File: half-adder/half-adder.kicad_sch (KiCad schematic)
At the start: 15 parts, among them J1 A, J2 B, J3 C, J4 5V, J5 GROUND, J6 CARRY OUT, J7 OUTPUT

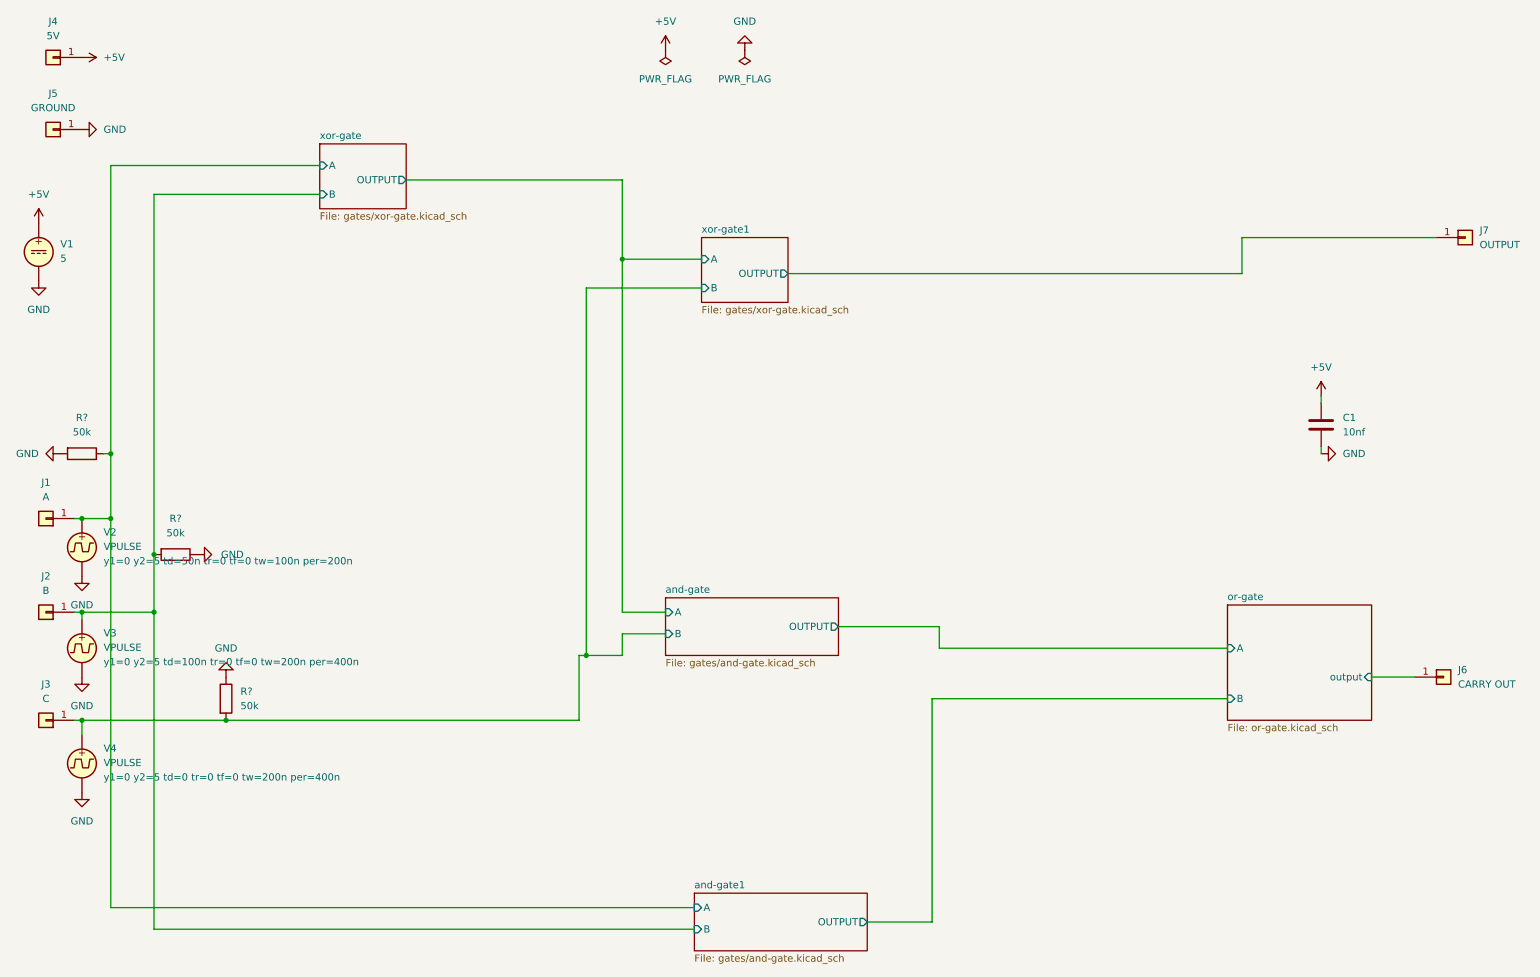
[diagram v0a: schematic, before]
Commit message: Fixed gates and moved half adder to its own directory
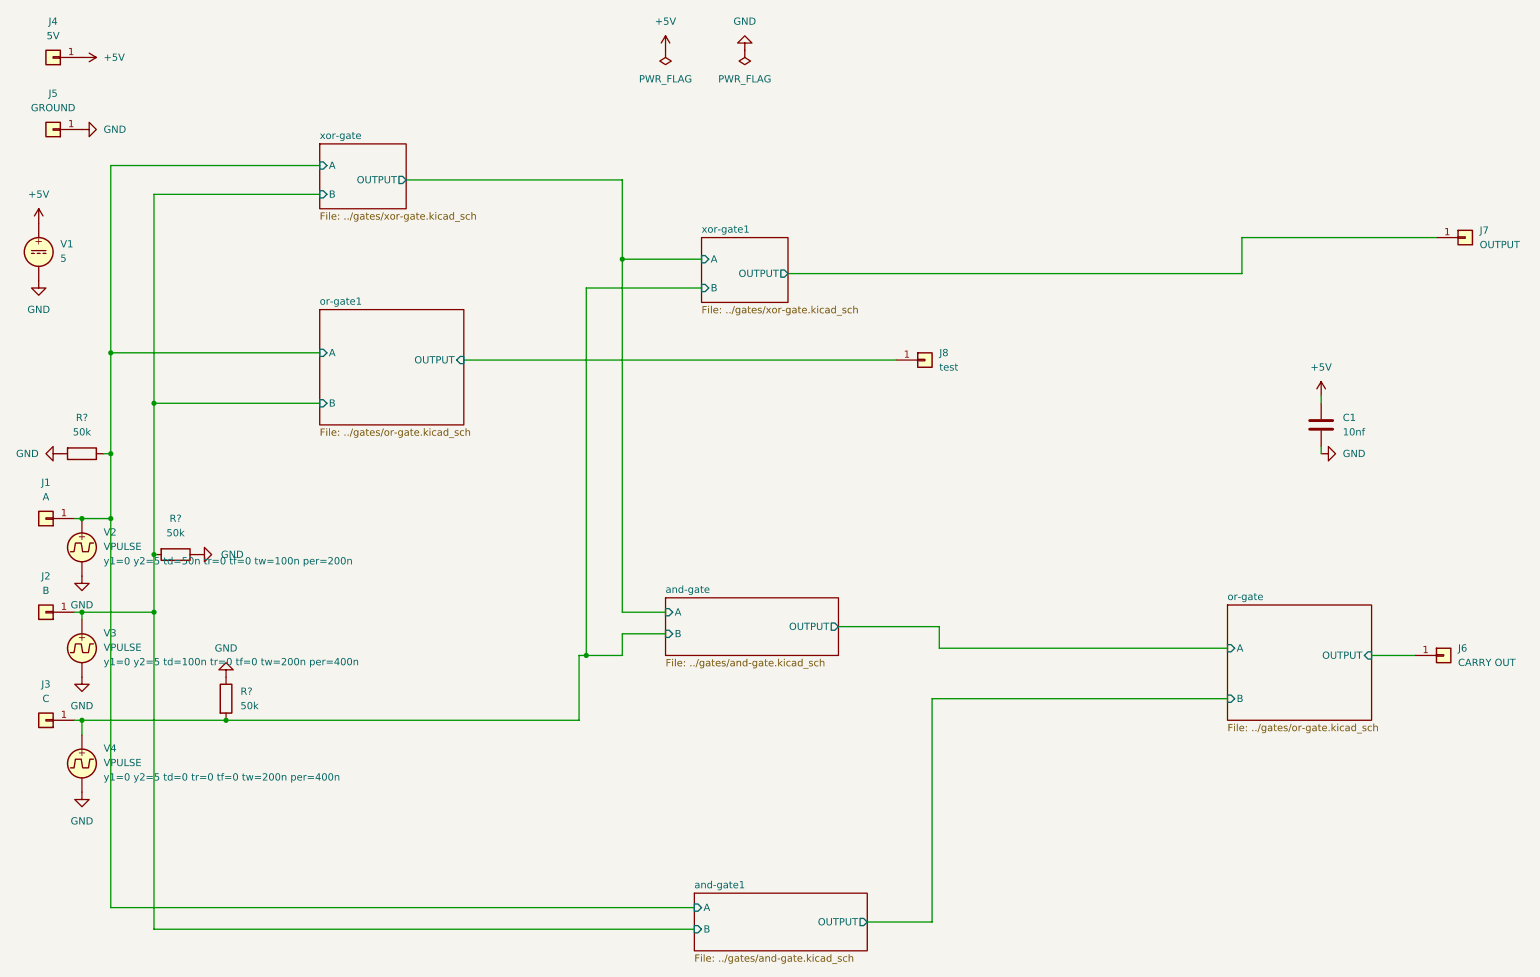
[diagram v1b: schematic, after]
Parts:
- added J8: test, Connector_PinHeader_2.54mm:PinHeader_1x01_P2.54mm_Vertical, symbol Connector_Generic:Conn_01x01
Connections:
- net or-gate/output renamed or-gate/OUTPUT
- new net or-gate1/OUTPUT: J8.1 (Pin_1)
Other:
- added sheet or-gate1 (../gates/or-gate.kicad_sch)
- sheet and-gate: file gates/and-gate.kicad_sch -> ../gates/and-gate.kicad_sch
- sheet and-gate1: file gates/and-gate.kicad_sch -> ../gates/and-gate.kicad_sch
- sheet or-gate: file or-gate.kicad_sch -> ../gates/or-gate.kicad_sch
- sheet or-gate ports: added OUTPUT; removed output
- sheet xor-gate: file gates/xor-gate.kicad_sch -> ../gates/xor-gate.kicad_sch
- sheet xor-gate1: file gates/xor-gate.kicad_sch -> ../gates/xor-gate.kicad_sch
- moved on the sheet: J6
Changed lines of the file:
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@@
 	)
 	(junction
+		(at 30.48 74.93)
+		(diameter 0)
+		(color 0 0 0 0)
+	)
+	(junction
 		(at 25.4 120.65)
 		(diameter 0)
@@
 	)
 	(junction
+		(at 38.1 83.82)
+		(diameter 0)
+		(color 0 0 0 0)
+	)
+	(junction
 		(at 114.3 128.27)
 		(diameter 0)
@@
 	(wire
 		(pts
-			(xy 38.1 46.99) (xy 38.1 110.49)
+			(xy 30.48 172.72) (xy 133.35 172.72)
 		)
 		(stroke
@@
 	(wire
 		(pts
-			(xy 30.48 172.72) (xy 133.35 172.72)
+			(xy 229.87 60.96) (xy 229.87 54.61)
 		)
 		(stroke
@@
 	(wire
 		(pts
-			(xy 229.87 60.96) (xy 229.87 54.61)
+			(xy 30.48 41.91) (xy 67.31 41.91)
 		)
 		(stroke
@@
 	(wire
 		(pts
-			(xy 30.48 41.91) (xy 67.31 41.91)
+			(xy 38.1 120.65) (xy 38.1 176.53)
 		)
 		(stroke
@@
 	(wire
 		(pts
-			(xy 38.1 120.65) (xy 38.1 176.53)
+			(xy 175.26 135.89) (xy 227.33 135.89)
 		)
 		(stroke
@@
 	(wire
 		(pts
-			(xy 175.26 135.89) (xy 227.33 135.89)
+			(xy 30.48 41.91) (xy 30.48 74.93)
 		)
 		(stroke
@@
 	(wire
 		(pts
-			(xy 30.48 41.91) (xy 30.48 92.71)
+			(xy 38.1 83.82) (xy 38.1 110.49)
 		)
 		(stroke
@@
 	(wire
 		(pts
+			(xy 67.31 74.93) (xy 30.48 74.93)
+		)
+		(stroke
+			(width 0)
+			(type default)
+		)
+	)
+	(wire
+		(pts
 			(xy 114.3 128.27) (xy 120.65 128.27)
 		)
@@
 	(wire
 		(pts
+			(xy 92.71 76.2) (xy 168.91 76.2)
+		)
+		(stroke
+			(width 0)
+			(type default)
+		)
+	)
+	(wire
+		(pts
 			(xy 50.8 139.7) (xy 113.03 139.7)
 		)
@@
 	(wire
 		(pts
-			(xy 252.73 132.08) (xy 260.35 132.08)
+			(xy 252.73 128.27) (xy 260.35 128.27)
 		)
 		(stroke
@@
 	(wire
 		(pts
+			(xy 38.1 83.82) (xy 67.31 83.82)
+		)
+		(stroke
+			(width 0)
+			(type default)
+		)
+	)
+	(wire
+		(pts
 			(xy 120.65 58.42) (xy 134.62 58.42)
 		)
@@
 	(wire
 		(pts
+			(xy 38.1 46.99) (xy 38.1 83.82)
+		)
+		(stroke
+			(width 0)
+			(type default)
+		)
+	)
+	(wire
+		(pts
 			(xy 25.4 120.65) (xy 38.1 120.65)
 		)
@@
 	(wire
 		(pts
+			(xy 30.48 74.93) (xy 30.48 92.71)
+		)
+		(stroke
+			(width 0)
+			(type default)
+		)
+	)
+	(wire
+		(pts
 			(xy 243.84 82.55) (xy 243.84 83.82)
 		)
@@
 	)
 	(symbol
+		(lib_id "Connector_Generic:Conn_01x01")
+		(at 173.99 76.2 0)
+		(unit 1)
+		(exclude_from_sim yes)
+		(in_bom yes)
+		(on_board yes)
+		(dnp no)
+		(fields_autoplaced yes)
+		(property "Reference" "J8"
+			(at 176.53 74.93 0)
+			(effects
+				(font
+					(size 1.27 1.27)
+				)
+				(justify left)
+			)
+		)
+		(property "Value" "test"
+			(at 176.53 77.47 0)
+			(effects
+				(font
+					(size 1.27 1.27)
+				)
+				(justify left)
+			)
+		)
+		(property "Footprint" "Connector_PinHeader_2.54mm:PinHeader_1x01_P2.54mm_Vertical"
+			(at 173.99 76.2 0)
+			(effects
+				(font
+					(size 1.27 1.27)
+				)
+				(hide yes)
+			)
+		)
+		(property "Datasheet" "~"
+			(at 173.99 76.2 0)
+			(effects
+				(font
+					(size 1.27 1.27)
+				)
+				(hide yes)
+			)
+		)
+		(property "Description" ""
+			(at 173.99 76.2 0)
+			(effects
+				(font
+					(size 1.27 1.27)
+				)
+				(hide yes)
+			)
+		)
+		(property "LCSC" ""
+			(at 173.99 76.2 0)
+			(effects
+				(font
+					(size 1.27 1.27)
+				)
+				(hide yes)
+			)
+		)
+		(pin "1"
+		)
+		(instances
+			(project "half-adder"
+				(path "/88c27409-0a88-4cf1-8b65-cf7271709e32"
+					(reference "J8")
+					(unit 1)
+				)
+			)
+		)
+	)
+	(symbol
 		(lib_id "power:+5V")
 		(at 25.4 22.86 270)
@@
 	(symbol
 		(lib_id "Connector_Generic:Conn_01x01")
-		(at 265.43 132.08 0)
+		(at 265.43 128.27 0)
 		(unit 1)
 		(exclude_from_sim yes)
@@
 		(fields_autoplaced yes)
 		(property "Reference" "J6"
-			(at 267.97 130.81 0)
+			(at 267.97 127 0)
 			(effects
 				(font
@@
 		)
 		(property "Value" "CARRY OUT"
-			(at 267.97 133.35 0)
+			(at 267.97 129.54 0)
 			(effects
 				(font
@@
 		)
 		(property "Footprint" "Connector_PinHeader_2.54mm:PinHeader_1x01_P2.54mm_Vertical"
-			(at 265.43 132.08 0)
+			(at 265.43 128.27 0)
 			(effects
 				(font
@@
 		)
 		(property "Datasheet" "~"
-			(at 265.43 132.08 0)
+			(at 265.43 128.27 0)
 			(effects
 				(font
@@
 		)
 		(property "Description" ""
-			(at 265.43 132.08 0)
+			(at 265.43 128.27 0)
 			(effects
 				(font
@@
 		)
 		(property "LCSC" ""
-			(at 265.43 132.08 0)
+			(at 265.43 128.27 0)
 			(effects
 				(font
@@
 			)
 		)
-		(property "Sheetfile" "gates/and-gate.kicad_sch"
+		(property "Sheetfile" "../gates/and-gate.kicad_sch"
 			(at 133.35 180.9246 0)
 			(effects
@@
 	)
 	(sheet
-		(at 227.33 119.38)
+		(at 67.31 67.31)
 		(size 25.4 20.32)
 		(fields_autoplaced yes)
@@
 			(color 0 0 0 0.0000)
 		)
-		(property "Sheetname" "or-gate"
-			(at 227.33 118.6684 0)
+		(property "Sheetname" "or-gate1"
+			(at 67.31 66.5984 0)
 			(effects
 				(font
@@
 			)
 		)
-		(property "Sheetfile" "or-gate.kicad_sch"
-			(at 227.33 140.2846 0)
+		(property "Sheetfile" "../gates/or-gate.kicad_sch"
+			(at 67.31 88.2146 0)
 			(effects
 				(font
@@
 			)
 		)
-		(pin "output" input
-			(at 252.73 132.08 0)
+		(pin "A" input
+			(at 67.31 74.93 180)
+			(effects
+				(font
+					(size 1.27 1.27)
+				)
+				(justify left)
+			)
+		)
+		(pin "B" input
+			(at 67.31 83.82 180)
+			(effects
+				(font
+					(size 1.27 1.27)
+				)
+				(justify left)
+			)
+		)
+		(pin "OUTPUT" input
+			(at 92.71 76.2 0)
 			(effects
 				(font
@@
 			)
 		)
+		(instances
+			(project "half-adder"
+				(path "/88c27409-0a88-4cf1-8b65-cf7271709e32"
+					(page "13")
+				)
+			)
+		)
+	)
+	(sheet
+		(at 227.33 119.38)
+		(size 25.4 20.32)
+		(fields_autoplaced yes)
+		(stroke
+			(width 0.1524)
+			(type solid)
+		)
+		(fill
+			(color 0 0 0 0.0000)
+		)
+		(property "Sheetname" "or-gate"
+			(at 227.33 118.6684 0)
+			(effects
+				(font
+					(size 1.27 1.27)
+				)
+				(justify left bottom)
+			)
+		)
+		(property "Sheetfile" "../gates/or-gate.kicad_sch"
+			(at 227.33 140.2846 0)
+			(effects
+				(font
+					(size 1.27 1.27)
+				)
+				(justify left top)
+			)
+		)
 		(pin "A" input
 			(at 227.33 127 180)
@@
 			)
 		)
+		(pin "OUTPUT" input
+			(at 252.73 128.27 0)
+			(effects
+				(font
+					(size 1.27 1.27)
+				)
+				(justify right)
+			)
+		)
 		(instances
 			(project "half-adder"
@@
 			)
 		)
-		(property "Sheetfile" "gates/xor-gate.kicad_sch"
+		(property "Sheetfile" "../gates/xor-gate.kicad_sch"
 			(at 67.31 50.1146 0)
 			(effects
@@
 			)
 		)
-		(property "Sheetfile" "gates/xor-gate.kicad_sch"
+		(property "Sheetfile" "../gates/xor-gate.kicad_sch"
 			(at 134.62 66.6246 0)
 			(effects
@@
 			)
 		)
-		(property "Sheetfile" "gates/and-gate.kicad_sch"
+		(property "Sheetfile" "../gates/and-gate.kicad_sch"
 			(at 128.27 128.8546 0)
 			(effects

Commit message: Remove unneeded or gate
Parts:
- removed J8: test, Connector_PinHeader_2.54mm:PinHeader_1x01_P2.54mm_Vertical, symbol Connector_Generic:Conn_01x01
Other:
- removed sheet or-gate1
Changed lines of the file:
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@@
-	)
-	(junction
-		(at 30.48 74.93)
-		(diameter 0)
-		(color 0 0 0 0)
 	)
 	(junction
@@
 	)
 	(junction
-		(at 38.1 83.82)
-		(diameter 0)
-		(color 0 0 0 0)
-	)
-	(junction
 		(at 114.3 128.27)
 		(diameter 0)
@@
 	(wire
 		(pts
-			(xy 30.48 41.91) (xy 30.48 74.93)
+			(xy 30.48 41.91) (xy 30.48 92.71)
 		)
 		(stroke
@@
 	(wire
 		(pts
-			(xy 38.1 83.82) (xy 38.1 110.49)
+			(xy 38.1 46.99) (xy 38.1 110.49)
 		)
 		(stroke
@@
 	(wire
 		(pts
-			(xy 67.31 74.93) (xy 30.48 74.93)
-		)
-		(stroke
-			(width 0)
-			(type default)
-		)
-	)
-	(wire
-		(pts
 			(xy 114.3 128.27) (xy 120.65 128.27)
 		)
@@
 	(wire
 		(pts
-			(xy 92.71 76.2) (xy 168.91 76.2)
-		)
-		(stroke
-			(width 0)
-			(type default)
-		)
-	)
-	(wire
-		(pts
 			(xy 50.8 139.7) (xy 113.03 139.7)
 		)
@@
 	(wire
 		(pts
-			(xy 38.1 83.82) (xy 67.31 83.82)
-		)
-		(stroke
-			(width 0)
-			(type default)
-		)
-	)
-	(wire
-		(pts
 			(xy 120.65 58.42) (xy 134.62 58.42)
 		)
@@
 	(wire
 		(pts
-			(xy 38.1 46.99) (xy 38.1 83.82)
-		)
-		(stroke
-			(width 0)
-			(type default)
-		)
-	)
-	(wire
-		(pts
 			(xy 25.4 120.65) (xy 38.1 120.65)
 		)
@@
 		(pts
 			(xy 38.1 176.53) (xy 133.35 176.53)
-		)
-		(stroke
-			(width 0)
-			(type default)
-		)
-	)
-	(wire
-		(pts
-			(xy 30.48 74.93) (xy 30.48 92.71)
 		)
 		(stroke
@@
 	)
 	(symbol
-		(lib_id "Connector_Generic:Conn_01x01")
-		(at 173.99 76.2 0)
-		(unit 1)
-		(exclude_from_sim yes)
-		(in_bom yes)
-		(on_board yes)
-		(dnp no)
-		(fields_autoplaced yes)
-		(property "Reference" "J8"
-			(at 176.53 74.93 0)
-			(effects
-				(font
-					(size 1.27 1.27)
-				)
-				(justify left)
-			)
-		)
-		(property "Value" "test"
-			(at 176.53 77.47 0)
-			(effects
-				(font
-					(size 1.27 1.27)
-				)
-				(justify left)
-			)
-		)
-		(property "Footprint" "Connector_PinHeader_2.54mm:PinHeader_1x01_P2.54mm_Vertical"
-			(at 173.99 76.2 0)
-			(effects
-				(font
-					(size 1.27 1.27)
-				)
-				(hide yes)
-			)
-		)
-		(property "Datasheet" "~"
-			(at 173.99 76.2 0)
-			(effects
-				(font
-					(size 1.27 1.27)
-				)
-				(hide yes)
-			)
-		)
-		(property "Description" ""
-			(at 173.99 76.2 0)
-			(effects
-				(font
-					(size 1.27 1.27)
-				)
-				(hide yes)
-			)
-		)
-		(property "LCSC" ""
-			(at 173.99 76.2 0)
-			(effects
-				(font
-					(size 1.27 1.27)
-				)
-				(hide yes)
-			)
-		)
-		(pin "1"
-		)
-		(instances
-			(project "half-adder"
-				(path "/88c27409-0a88-4cf1-8b65-cf7271709e32"
-					(reference "J8")
-					(unit 1)
-				)
-			)
-		)
-	)
-	(symbol
 		(lib_id "power:+5V")
 		(at 25.4 22.86 270)
@@
 				)
 			)
-		)
-	)
-	(sheet
-		(at 67.31 67.31)
-		(size 25.4 20.32)
-		(fields_autoplaced yes)
-		(stroke
-			(width 0.1524)
-			(type solid)
-		)
-		(fill
-			(color 0 0 0 0.0000)
-		)
-		(property "Sheetname" "or-gate1"
-			(at 67.31 66.5984 0)
-			(effects
-				(font
-					(size 1.27 1.27)
-				)
-				(justify left bottom)
-			)
-		)
-		(property "Sheetfile" "../gates/or-gate.kicad_sch"
-			(at 67.31 88.2146 0)
-			(effects
-				(font
-					(size 1.27 1.27)
-				)
-				(justify left top)
-			)
-		)
-		(pin "A" input
-			(at 67.31 74.93 180)
-			(effects
-				(font
-					(size 1.27 1.27)
-				)
-				(justify left)
-			)
-		)
-		(pin "B" input
-			(at 67.31 83.82 180)
-			(effects
-				(font
-					(size 1.27 1.27)
-				)
-				(justify left)
-			)
-		)
-		(pin "OUTPUT" input
-			(at 92.71 76.2 0)
-			(effects
-				(font
-					(size 1.27 1.27)
-				)
-				(justify right)
-			)
-		)
-		(instances
-			(project "half-adder"
-				(path "/88c27409-0a88-4cf1-8b65-cf7271709e32"
-					(page "13")
-				)
-			)

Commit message: Remove capacitor connected to 5V and gnd
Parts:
- removed C1: 10nf, symbol Device:C
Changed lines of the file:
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@@
 	(wire
 		(pts
-			(xy 243.84 92.71) (xy 243.84 91.44)
+			(xy 114.3 128.27) (xy 113.03 128.27)
 		)
 		(stroke
@@
 	(wire
 		(pts
-			(xy 114.3 128.27) (xy 113.03 128.27)
+			(xy 120.65 58.42) (xy 134.62 58.42)
 		)
 		(stroke
@@
 	(wire
 		(pts
-			(xy 120.65 58.42) (xy 134.62 58.42)
+			(xy 25.4 120.65) (xy 25.4 121.92)
 		)
 		(stroke
@@
 	(wire
 		(pts
-			(xy 25.4 120.65) (xy 25.4 121.92)
+			(xy 24.13 139.7) (xy 25.4 139.7)
 		)
 		(stroke
@@
 	(wire
 		(pts
-			(xy 24.13 139.7) (xy 25.4 139.7)
+			(xy 24.13 104.14) (xy 25.4 104.14)
 		)
 		(stroke
@@
 	(wire
 		(pts
-			(xy 24.13 104.14) (xy 25.4 104.14)
+			(xy 24.13 120.65) (xy 25.4 120.65)
 		)
 		(stroke
@@
 	(wire
 		(pts
-			(xy 24.13 120.65) (xy 25.4 120.65)
+			(xy 30.48 92.71) (xy 30.48 104.14)
 		)
 		(stroke
@@
 	(wire
 		(pts
-			(xy 30.48 92.71) (xy 30.48 104.14)
+			(xy 38.1 46.99) (xy 67.31 46.99)
 		)
 		(stroke
@@
 	(wire
 		(pts
-			(xy 38.1 46.99) (xy 67.31 46.99)
+			(xy 25.4 120.65) (xy 38.1 120.65)
 		)
 		(stroke
@@
 	(wire
 		(pts
-			(xy 25.4 120.65) (xy 38.1 120.65)
+			(xy 38.1 176.53) (xy 133.35 176.53)
 		)
 		(stroke
@@
 	(wire
 		(pts
-			(xy 38.1 176.53) (xy 133.35 176.53)
+			(xy 113.03 139.7) (xy 113.03 128.27)
 		)
 		(stroke
@@
 	(wire
 		(pts
-			(xy 243.84 82.55) (xy 243.84 83.82)
+			(xy 25.4 142.24) (xy 25.4 139.7)
 		)
 		(stroke
@@
 		)
 	)
-	(wire
-		(pts
-			(xy 113.03 139.7) (xy 113.03 128.27)
-		)
-		(stroke
-			(width 0)
-			(type default)
-		)
-	)
-	(wire
-		(pts
-			(xy 25.4 142.24) (xy 25.4 139.7)
-		)
-		(stroke
-			(width 0)
-			(type default)
-		)
-	)
 	(symbol
 		(lib_id "Simulation_SPICE:VPULSE")
@@
 	)
 	(symbol
-		(lib_id "power:GND")
-		(at 243.84 92.71 90)
-		(unit 1)
-		(exclude_from_sim no)
-		(in_bom yes)
-		(on_board yes)
-		(dnp no)
-		(fields_autoplaced yes)
-		(property "Reference" "#PWR014"
-			(at 250.19 92.71 0)
-			(effects
-				(font
-					(size 1.27 1.27)
-				)
-				(hide yes)
-			)
-		)
-		(property "Value" "GND"
-			(at 247.65 92.7099 90)
-			(effects
-				(font
-					(size 1.27 1.27)
-				)
-				(justify right)
-			)
-		)
-		(property "Footprint" ""
-			(at 243.84 92.71 0)
-			(effects
-				(font
-					(size 1.27 1.27)
-				)
-				(hide yes)
-			)
-		)
-		(property "Datasheet" ""
-			(at 243.84 92.71 0)
-			(effects
-				(font
-					(size 1.27 1.27)
-				)
-				(hide yes)
-			)
-		)
-		(property "Description" ""
-			(at 243.84 92.71 0)
-			(effects
-				(font
-					(size 1.27 1.27)
-				)
-				(hide yes)
-			)
-		)
-		(pin "1"
-		)
-		(instances
-			(project "half-adder"
-				(path "/88c27409-0a88-4cf1-8b65-cf7271709e32"
-					(reference "#PWR014")
-					(unit 1)
-				)
-			)
-		)
-	)
-	(symbol
 		(lib_id "power:PWR_FLAG")
 		(at 128.27 21.59 180)
@@
 	)
 	(symbol
-		(lib_id "power:+5V")
-		(at 243.84 82.55 0)
-		(unit 1)
-		(exclude_from_sim no)
-		(in_bom yes)
-		(on_board yes)
-		(dnp no)
-		(fields_autoplaced yes)
-		(property "Reference" "#PWR013"
-			(at 243.84 86.36 0)
-			(effects
-				(font
-					(size 1.27 1.27)
-				)
-				(hide yes)
-			)
-		)
-		(property "Value" "+5V"
-			(at 243.84 77.47 0)
-			(effects
-				(font
-					(size 1.27 1.27)
-				)
-			)
-		)
-		(property "Footprint" ""
-			(at 243.84 82.55 0)
-			(effects
-				(font
-					(size 1.27 1.27)
-				)
-				(hide yes)
-			)
-		)
-		(property "Datasheet" ""
-			(at 243.84 82.55 0)
-			(effects
-				(font
-					(size 1.27 1.27)
-				)
-				(hide yes)
-			)
-		)
-		(property "Description" ""
-			(at 243.84 82.55 0)
-			(effects
-				(font
-					(size 1.27 1.27)
-				)
-				(hide yes)
-			)
-		)
-		(pin "1"
-		)
-		(instances
-			(project "half-adder"
-				(path "/88c27409-0a88-4cf1-8b65-cf7271709e32"
-					(reference "#PWR013")
-					(unit 1)
-				)
-			)
-		)
-	)
-	(symbol
 		(lib_id "Connector_Generic:Conn_01x01")
 		(at 20.32 35.56 180)
@@
 					(unit 1)
 				)
-			)
-		)
-	)
-	(symbol
-		(lib_id "Device:C")
-		(at 243.84 87.63 0)
-		(unit 1)
-		(exclude_from_sim no)
-		(in_bom yes)
-		(on_board yes)
-		(dnp no)
-		(fields_autoplaced yes)
-		(property "Reference" "C1"
-			(at 247.65 86.3599 0)
-			(effects
-				(font
-					(size 1.27 1.27)
-				)
-				(justify left)
-			)
-		)
-		(property "Value" "10nf"
-			(at 247.65 88.8999 0)
-			(effects
-				(font
-					(size 1.27 1.27)
-				)
-				(justify left)
-			)
-		)
-		(property "Footprint" ""
-			(at 244.8052 91.44 0)
-			(effects
-				(font
-					(size 1.27 1.27)
-				)
-				(hide yes)
-			)
-		)
-		(property "Datasheet" "~"
-			(at 243.84 87.63 0)
-			(effects
-				(font
-					(size 1.27 1.27)
-				)
-				(hide yes)
-			)
-		)
-		(property "Description" "Unpolarized capacitor"
-			(at 243.84 87.63 0)
-			(effects
-				(font
-					(size 1.27 1.27)
-				)
-				(hide yes)
-			)
-		)
-		(pin "1"
-		)
-		(pin "2"
-		)
-		(instances
-			(project ""
-				(path "/88c27409-0a88-4cf1-8b65-cf7271709e32"
-					(reference "C1")
-					(unit 1)
-				)
